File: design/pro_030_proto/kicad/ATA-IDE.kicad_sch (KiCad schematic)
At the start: 26 parts, among them IC11 ATF22V10C, IC12 74HCT245, IC20 ATF750, IC21 74HCT241, IC9 74HCT245, J26 IDE_LED, J27 Conn_02x20_Odd_Even, J28 Conn_02x22_Odd_Even, Q2 2N3906

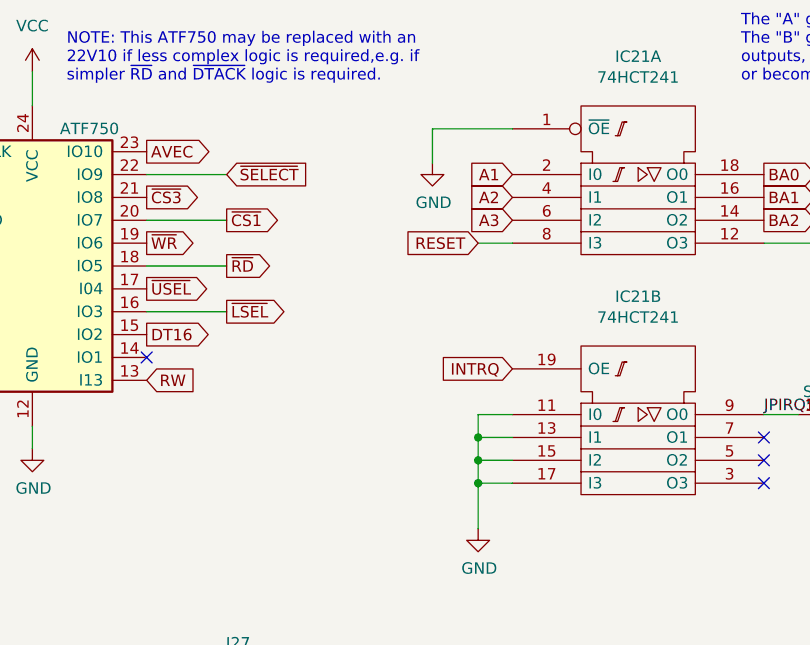
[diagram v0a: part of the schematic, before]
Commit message: Fix wrong A lines, add INTRQ pulldown
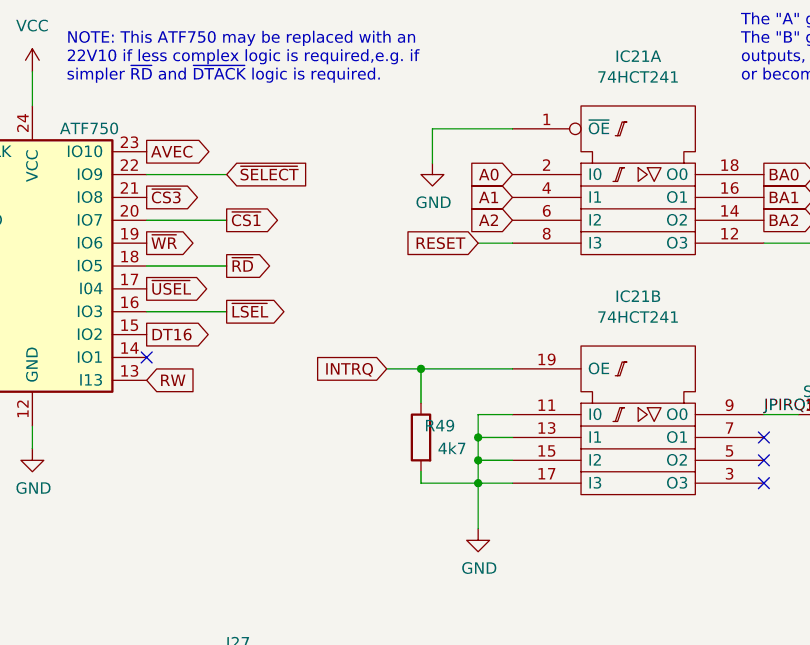
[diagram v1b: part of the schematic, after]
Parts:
- added R49: 4k7, rosco_m68k:R-0207_10, symbol Device:R
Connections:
- net A0: now also IC21.2 (I0)
- net A1: now also IC21.4 (I1); no longer IC21.2 (I0)
- net A2: now also IC21.6 (I2); no longer IC21.4 (I1)
- net A3: no longer IC21.6 (I2)
- net GND: now also R49.2
- net INTRQ: now also R49.1
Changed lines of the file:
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@@
   (junction (at 212.09 76.2) (diameter 0) (color 0 0 0 0)
+  )
+  (junction (at 205.74 66.04) (diameter 0) (color 0 0 0 0)
   )
   (junction (at 212.09 78.74) (diameter 0) (color 0 0 0 0)
@@
     (stroke (width 0) (type default) (color 0 0 0 0))
   )
+  (wire (pts (xy 205.74 66.04) (xy 215.9 66.04))
+    (stroke (width 0) (type default) (color 0 0 0 0))
+  )
   (wire (pts (xy 276.86 129.54) (xy 276.86 134.62))
     (stroke (width 0) (type default) (color 0 0 0 0))
   )
+  (wire (pts (xy 201.93 66.04) (xy 205.74 66.04))
+    (stroke (width 0) (type default) (color 0 0 0 0))
+  )
   (wire (pts (xy 121.92 179.07) (xy 133.35 179.07))
     (stroke (width 0) (type default) (color 0 0 0 0))
@@
     (stroke (width 0) (type default) (color 0 0 0 0))
   )
+  (wire (pts (xy 205.74 78.74) (xy 212.09 78.74))
+    (stroke (width 0) (type default) (color 0 0 0 0))
+  )
   (wire (pts (xy 143.51 161.29) (xy 140.97 161.29))
     (stroke (width 0) (type default) (color 0 0 0 0))
@@
     (stroke (width 0) (type default) (color 0 0 0 0))
   )
+  (wire (pts (xy 205.74 77.47) (xy 205.74 78.74))
+    (stroke (width 0) (type default) (color 0 0 0 0))
+  )
   (wire (pts (xy 266.7 157.48) (xy 266.7 149.86))
     (stroke (width 0) (type default) (color 0 0 0 0))
@@
   )
   (wire (pts (xy 215.9 71.12) (xy 212.09 71.12))
+    (stroke (width 0) (type default) (color 0 0 0 0))
+  )
+  (wire (pts (xy 205.74 66.04) (xy 205.74 69.85))
     (stroke (width 0) (type default) (color 0 0 0 0))
   )
@@
     )
   )
-  (global_label "A1" (shape input) (at 215.9 44.45 180) (fields_autoplaced)
-    (effects (font (size 1.27 1.27)) (justify right))
-    (property "Intersheet References" "${INTERSHEET_REFS}" (id 0) (at 0 0 0)
-      (effects (font (size 1.27 1.27)) hide)
+  (global_label "A0" (shape input) (at 215.9 44.45 180) (fields_autoplaced)
+    (effects (font (size 1.27 1.27)) (justify right))
+    (property "Intersheet References" "${INTERSHEET_REFS}" (id 0) (at 211.2777 44.3706 0)
+      (effects (font (size 1.27 1.27)) (justify right) hide)
     )
   )
@@
     )
   )
-  (global_label "INTRQ" (shape input) (at 215.9 66.04 180) (fields_autoplaced)
-    (effects (font (size 1.27 1.27)) (justify right))
-    (property "Intersheet References" "${INTERSHEET_REFS}" (id 0) (at 0 0 0)
+  (global_label "INTRQ" (shape input) (at 201.93 66.04 180) (fields_autoplaced)
+    (effects (font (size 1.27 1.27)) (justify right))
+    (property "Intersheet References" "${INTERSHEET_REFS}" (id 0) (at -13.97 0 0)
       (effects (font (size 1.27 1.27)) hide)
     )
@@
     )
   )
-  (global_label "A3" (shape input) (at 215.9 49.53 180) (fields_autoplaced)
-    (effects (font (size 1.27 1.27)) (justify right))
-    (property "Intersheet References" "${INTERSHEET_REFS}" (id 0) (at 0 0 0)
-      (effects (font (size 1.27 1.27)) hide)
+  (global_label "A2" (shape input) (at 215.9 49.53 180) (fields_autoplaced)
+    (effects (font (size 1.27 1.27)) (justify right))
+    (property "Intersheet References" "${INTERSHEET_REFS}" (id 0) (at 211.2777 49.4506 0)
+      (effects (font (size 1.27 1.27)) (justify right) hide)
     )
   )
@@
     )
   )
-  (global_label "A2" (shape input) (at 215.9 46.99 180) (fields_autoplaced)
-    (effects (font (size 1.27 1.27)) (justify right))
-    (property "Intersheet References" "${INTERSHEET_REFS}" (id 0) (at 0 0 0)
-      (effects (font (size 1.27 1.27)) hide)
+  (global_label "A1" (shape input) (at 215.9 46.99 180) (fields_autoplaced)
+    (effects (font (size 1.27 1.27)) (justify right))
+    (property "Intersheet References" "${INTERSHEET_REFS}" (id 0) (at 211.2777 46.9106 0)
+      (effects (font (size 1.27 1.27)) (justify right) hide)
     )
   )
@@
     (pin "1")
   )
+  (symbol (lib_id "Device:R") (at 205.74 73.66 0) (mirror y) (unit 1)
+    (in_bom yes) (on_board yes)
+    (property "Reference" "R49" (id 0) (at 209.55 72.39 0)
+      (effects (font (size 1.27 1.27)) (justify left))
+    )
+    (property "Value" "4k7" (id 1) (at 210.82 74.93 0)
+      (effects (font (size 1.27 1.27)) (justify left))
+    )
+    (property "Footprint" "rosco_m68k:R-0207_10" (id 2) (at 207.518 73.66 90)
+      (effects (font (size 1.27 1.27)) hide)
+    )
+    (property "Datasheet" "~" (id 3) (at 205.74 73.66 0)
+      (effects (font (size 1.27 1.27)) hide)
+    )
+    (pin "1")
+    (pin "2")
+  )
   (symbol (lib_id "power:VCC") (at 133.35 148.59 0) (unit 1)

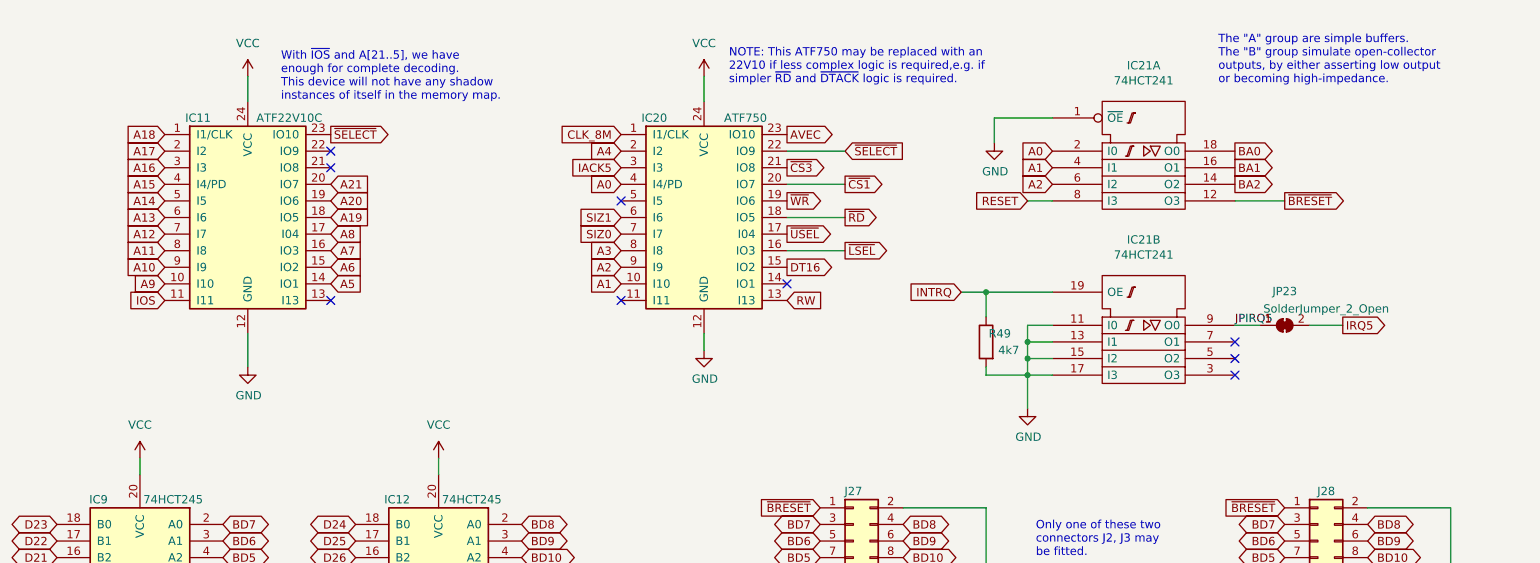
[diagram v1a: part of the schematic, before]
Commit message: Merge IDE decoder with main IO select on IC7
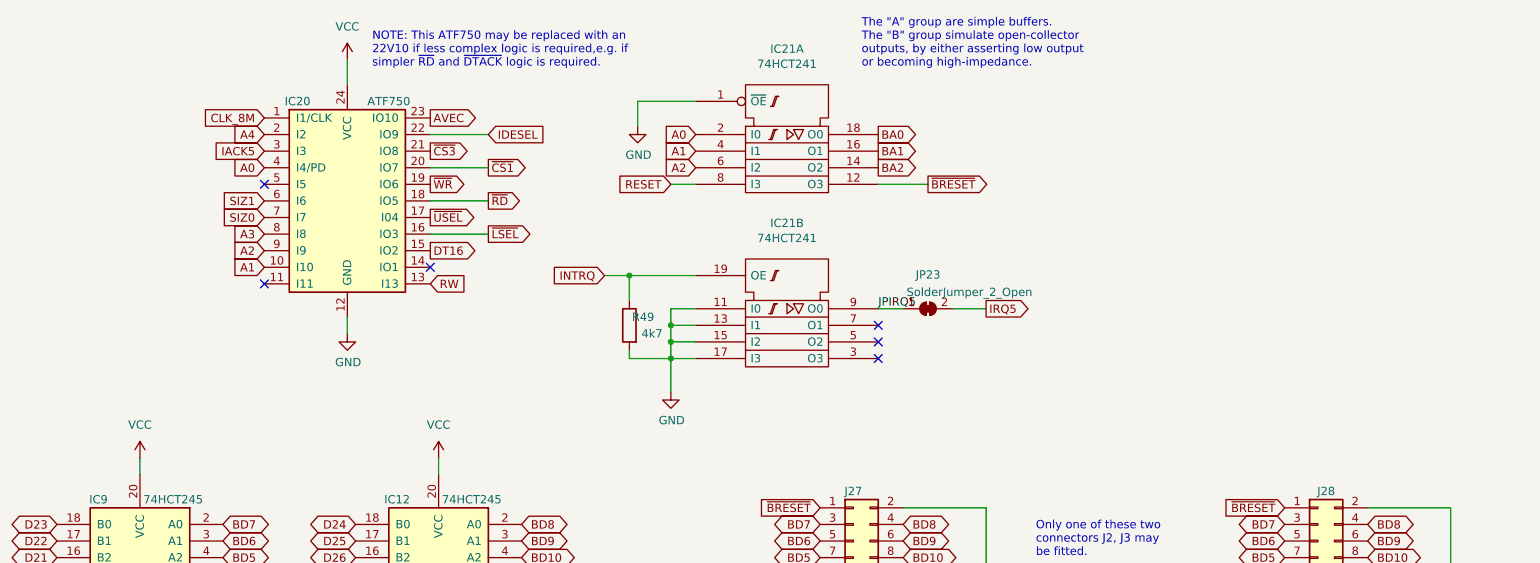
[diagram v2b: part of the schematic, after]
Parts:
- removed IC11: ATF22V10C, Package_DIP:DIP-24_W7.62mm_Socket_LongPads, symbol rosco_m68k:GAL22V10
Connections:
- net ~{SELECT} renamed IDESEL
- no-connect marks 19 -> 16
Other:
- note removed: "With ~{IOS} and A[21..5], we have enough for complete decoding. This device will not have any shadow instances of itself in the memory map."
- moved on the sheet: IC20, IC21A, IC21B, JP23, R49
